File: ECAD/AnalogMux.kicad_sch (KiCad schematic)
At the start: 3 parts, among them U5 NC7SB3157P6X, U6 NC7SB3157P6X, U7 NC7SB3157P6X

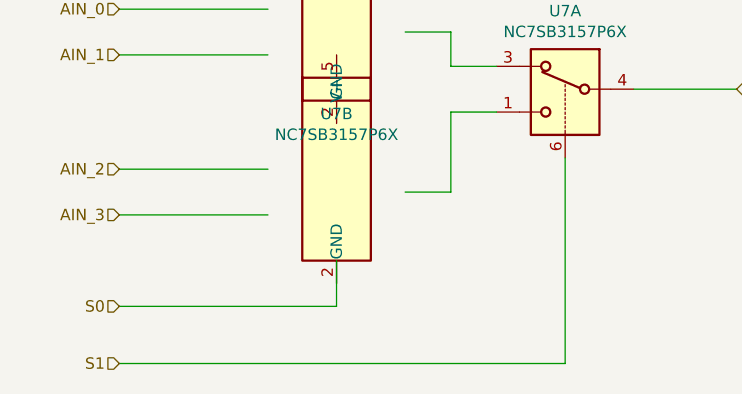
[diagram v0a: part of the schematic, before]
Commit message: pcb layout has started, still ned to make 5V to 3.3V power supply, add dip switch do individually control input power of each switch, 5V or 12V
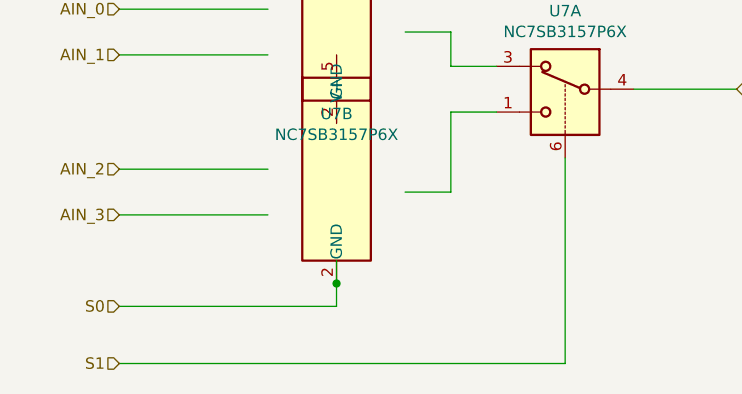
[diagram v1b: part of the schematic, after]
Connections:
- net S0: now also U7.2 (GND)
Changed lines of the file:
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@@
   (junction (at 99.06 33.02) (diameter 0.9144) (color 0 0 0 0))
   (junction (at 99.06 63.5) (diameter 0.9144) (color 0 0 0 0))
+  (junction (at 110.49 120.65) (diameter 0.9144) (color 0 0 0 0))
   (junction (at 124.46 33.02) (diameter 0.9144) (color 0 0 0 0))
   (wire (pts (xy 83.82 63.5) (xy 99.06 63.5))
@@
     (stroke (width 0) (type solid) (color 0 0 0 0))
   )
-  (wire (pts (xy 110.49 118.11) (xy 110.49 123.19))
+  (wire (pts (xy 110.49 118.11) (xy 110.49 120.65))
     (stroke (width 0) (type solid) (color 0 0 0 0))
   )
+  (wire (pts (xy 110.49 120.65) (xy 110.49 123.19))
+    (stroke (width 0) (type solid) (color 0 0 0 0))
+  )

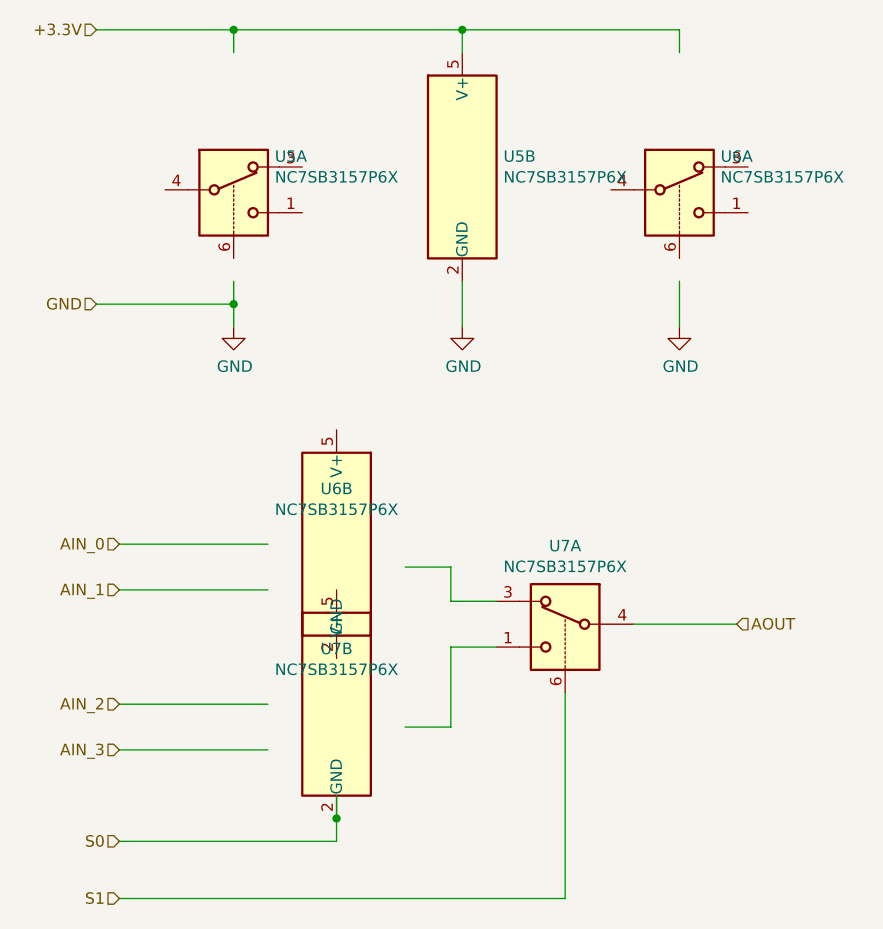
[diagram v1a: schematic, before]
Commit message: finishing up pcb, only billonly bill of materials need to be done to be compatible with lc from jlcpcb
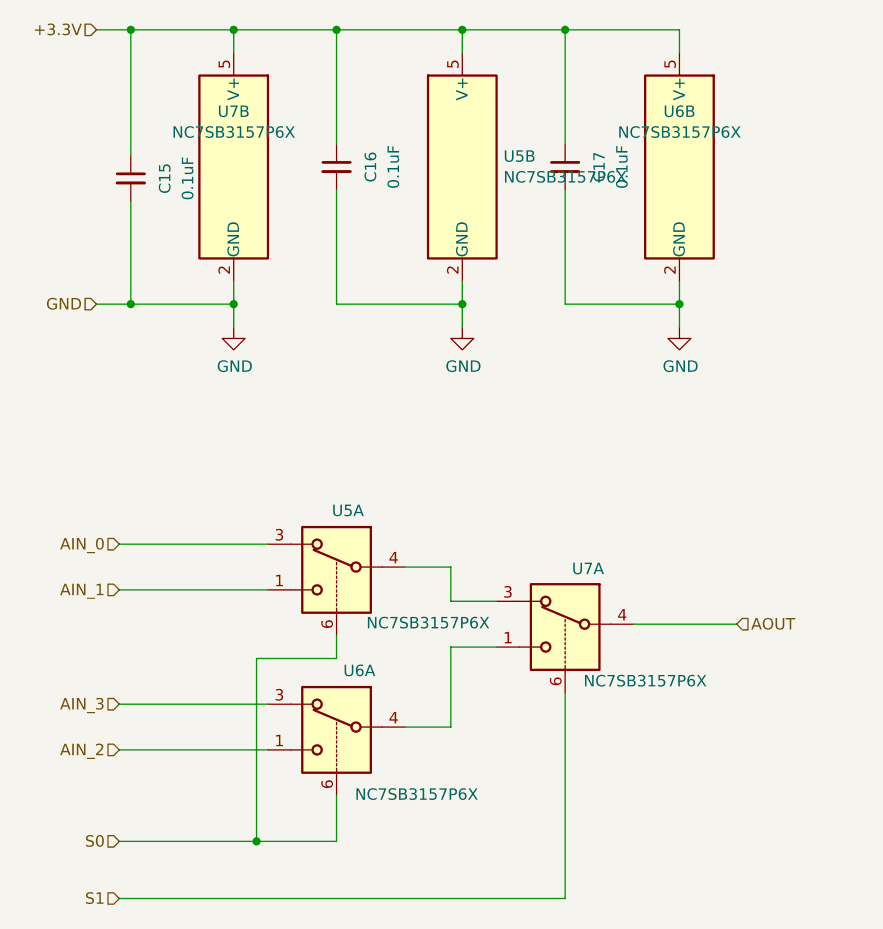
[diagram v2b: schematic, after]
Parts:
- added C15, C16, C17: 0.1uF, Capacitor_SMD:C_0603_1608Metric, symbol Device:C_Small
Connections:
- net +3.3V: now also U6.5 (V+), U7.5 (V+), C15.1, C16.1, C17.1
- net AIN_0: now also U5.3
- net AIN_1: now also U5.1
- net AIN_2: now also U6.1
- net AIN_3: now also U6.3
- net GND: now also U6.2 (GND), U7.2 (GND), C15.2, C16.2, C17.2
- net S0: now also U5.6, U6.6; no longer U7.2 (GND)
- net at U7.1: now also U6.4
- net at U7.3: now also U5.4
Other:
- moved on the sheet: U5A, U6A, U6B, U7B

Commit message: BOM fixed, ready to order
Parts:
- C15, C16, C17: Manufacturer (none) -> CCTC; Manufacturer Number (none) -> TCC0603X7R104K500CT
- U5, U6, U7: Manufacturer (none) -> ON Semiconductor; Manufacturer Number (none) -> NC7SB3157P6X
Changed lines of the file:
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@@
       (effects (font (size 1.27 1.27)) hide)
     )
-    (property "Datasheet" "~" (id 3) (at 87.63 49.53 0)
+    (property "Datasheet" "https://datasheet.lcsc.com/lcsc/1810181652_CCTC-TCC0603X7R104K500CT_C282519.pdf" (id 3) (at 87.63 49.53 0)
+      (effects (font (size 1.27 1.27)) hide)
+    )
+    (property "Manufacturer" "CCTC" (id 4) (at 87.63 49.53 0)
+      (effects (font (size 1.27 1.27)) hide)
+    )
+    (property "Manufacturer Number" "TCC0603X7R104K500CT" (id 5) (at 87.63 49.53 0)
       (effects (font (size 1.27 1.27)) hide)
     )
@@
       (effects (font (size 1.27 1.27)) hide)
     )
-    (property "Datasheet" "~" (id 3) (at 110.49 48.26 0)
+    (property "Datasheet" "https://datasheet.lcsc.com/lcsc/1810181652_CCTC-TCC0603X7R104K500CT_C282519.pdf" (id 3) (at 110.49 48.26 0)
+      (effects (font (size 1.27 1.27)) hide)
+    )
+    (property "Manufacturer" "CCTC" (id 4) (at 110.49 48.26 0)
+      (effects (font (size 1.27 1.27)) hide)
+    )
+    (property "Manufacturer Number" "TCC0603X7R104K500CT" (id 5) (at 110.49 48.26 0)
       (effects (font (size 1.27 1.27)) hide)
     )
@@
       (effects (font (size 1.27 1.27)) hide)
     )
-    (property "Datasheet" "~" (id 3) (at 135.89 48.26 0)
+    (property "Datasheet" "https://datasheet.lcsc.com/lcsc/1810181652_CCTC-TCC0603X7R104K500CT_C282519.pdf" (id 3) (at 135.89 48.26 0)
+      (effects (font (size 1.27 1.27)) hide)
+    )
+    (property "Manufacturer" "CCTC" (id 4) (at 135.89 48.26 0)
+      (effects (font (size 1.27 1.27)) hide)
+    )
+    (property "Manufacturer Number" "TCC0603X7R104K500CT" (id 5) (at 135.89 48.26 0)
       (effects (font (size 1.27 1.27)) hide)
     )
@@
     )
     (property "Datasheet" "https://www.onsemi.com/pub/Collateral/NC7SB3157-D.PDF" (id 3) (at 110.49 90.17 0)
+      (effects (font (size 1.27 1.27)) hide)
+    )
+    (property "Manufacturer" "ON Semiconductor" (id 4) (at 110.49 90.17 0)
+      (effects (font (size 1.27 1.27)) hide)
+    )
+    (property "Manufacturer Number" "NC7SB3157P6X" (id 5) (at 110.49 90.17 0)
       (effects (font (size 1.27 1.27)) hide)
     )
@@
       (effects (font (size 1.27 1.27)) hide)
     )
+    (property "Manufacturer" "ON Semiconductor" (id 4) (at 110.49 107.95 0)
+      (effects (font (size 1.27 1.27)) hide)
+    )
+    (property "Manufacturer Number" "NC7SB3157P6X" (id 5) (at 110.49 107.95 0)
+      (effects (font (size 1.27 1.27)) hide)
+    )
     (pin "1")
     (pin "3")
@@
       (effects (font (size 1.27 1.27)) hide)
     )
+    (property "Manufacturer" "ON Semiconductor" (id 4) (at 135.89 96.52 0)
+      (effects (font (size 1.27 1.27)) hide)
+    )
+    (property "Manufacturer Number" "NC7SB3157P6X" (id 5) (at 135.89 96.52 0)
+      (effects (font (size 1.27 1.27)) hide)
+    )
     (pin "1")
     (pin "3")
@@
     )
     (property "Datasheet" "https://www.onsemi.com/pub/Collateral/NC7SB3157-D.PDF" (id 3) (at 99.06 48.26 0)
+      (effects (font (size 1.27 1.27)) hide)
+    )
+    (property "Manufacturer" "ON Semiconductor" (id 4) (at 99.06 48.26 0)
+      (effects (font (size 1.27 1.27)) hide)
+    )
+    (property "Manufacturer Number" "NC7SB3157P6X" (id 5) (at 99.06 48.26 0)
       (effects (font (size 1.27 1.27)) hide)
     )
@@
       (effects (font (size 1.27 1.27)) hide)
     )
+    (property "Manufacturer" "ON Semiconductor" (id 4) (at 124.46 48.26 0)
+      (effects (font (size 1.27 1.27)) hide)
+    )
+    (property "Manufacturer Number" "NC7SB3157P6X" (id 5) (at 124.46 48.26 0)
+      (effects (font (size 1.27 1.27)) hide)
+    )
     (pin "2")
     (pin "5")
@@
       (effects (font (size 1.27 1.27)) hide)
     )
+    (property "Manufacturer" "ON Semiconductor" (id 4) (at 148.59 48.26 0)
+      (effects (font (size 1.27 1.27)) hide)
+    )
+    (property "Manufacturer Number" "NC7SB3157P6X" (id 5) (at 148.59 48.26 0)
+      (effects (font (size 1.27 1.27)) hide)
+    )

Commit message: adding production and step files
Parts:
- C15, C16, C17: Package (none) -> 0603
- U5, U6, U7: Package (none) -> SC-70-6(SOT-363)
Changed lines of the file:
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@@
     (effects (font (size 1.27 1.27)) (justify right))
   )
-  (hierarchical_label "AOUT" (shape input) (at 154.94 99.06 0)
+  (hierarchical_label "AOUT" (shape output) (at 154.94 99.06 0)
     (effects (font (size 1.27 1.27)) (justify left))
   )
@@
       (effects (font (size 1.27 1.27)) hide)
     )
+    (property "Package" "0603" (id 4) (at 87.63 49.53 0)
+      (effects (font (size 1.27 1.27)) hide)
+    )
     (pin "1")
     (pin "2")
@@
       (effects (font (size 1.27 1.27)) hide)
     )
+    (property "Package" "0603" (id 4) (at 110.49 48.26 0)
+      (effects (font (size 1.27 1.27)) hide)
+    )
     (pin "1")
     (pin "2")
@@
       (effects (font (size 1.27 1.27)) hide)
     )
+    (property "Package" "0603" (id 4) (at 135.89 48.26 0)
+      (effects (font (size 1.27 1.27)) hide)
+    )
     (pin "1")
     (pin "2")
@@
     )
     (property "Manufacturer Number" "NC7SB3157P6X" (id 5) (at 110.49 90.17 0)
+      (effects (font (size 1.27 1.27)) hide)
+    )
+    (property "Package" "SC-70-6(SOT-363)" (id 4) (at 110.49 90.17 0)
       (effects (font (size 1.27 1.27)) hide)
     )
@@
       (effects (font (size 1.27 1.27)) hide)
     )
+    (property "Package" "SC-70-6(SOT-363)" (id 4) (at 110.49 107.95 0)
+      (effects (font (size 1.27 1.27)) hide)
+    )
     (pin "1")
     (pin "3")
@@
       (effects (font (size 1.27 1.27)) hide)
     )
+    (property "Package" "SC-70-6(SOT-363)" (id 4) (at 135.89 96.52 0)
+      (effects (font (size 1.27 1.27)) hide)
+    )
     (pin "1")
     (pin "3")
@@
       (effects (font (size 1.27 1.27)) hide)
     )
+    (property "Package" "SC-70-6(SOT-363)" (id 4) (at 99.06 48.26 0)
+      (effects (font (size 1.27 1.27)) hide)
+    )
     (pin "2")
     (pin "5")
@@
     )
     (property "Manufacturer Number" "NC7SB3157P6X" (id 5) (at 124.46 48.26 0)
+      (effects (font (size 1.27 1.27)) hide)
+    )
+    (property "Package" "SC-70-6(SOT-363)" (id 4) (at 124.46 48.26 0)
       (effects (font (size 1.27 1.27)) hide)
     )
@@
       (effects (font (size 1.27 1.27)) hide)
     )
+    (property "Package" "SC-70-6(SOT-363)" (id 4) (at 148.59 48.26 0)
+      (effects (font (size 1.27 1.27)) hide)
+    )
